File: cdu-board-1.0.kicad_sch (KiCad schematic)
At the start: 18 parts, among them J1 Conn_01x02_Socket, J2 Conn_01x03_Socket, J3 Conn_01x02_Socket, Q1 TIP220G, Q2 TIP220G

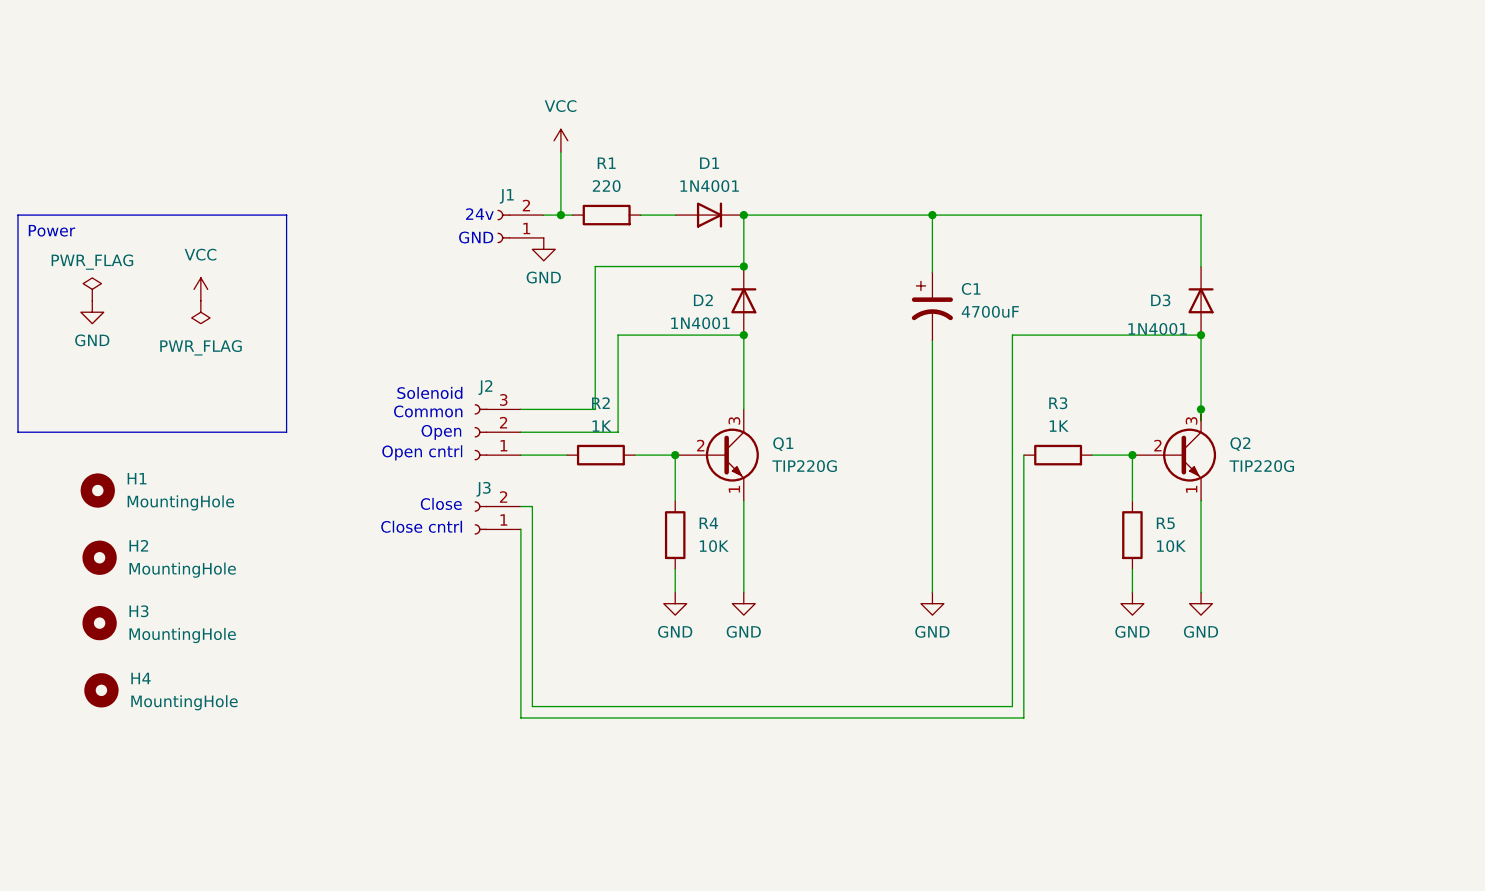
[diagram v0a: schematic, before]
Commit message: Fixed transistor - v1.0 used TIP220G and not TIP120G
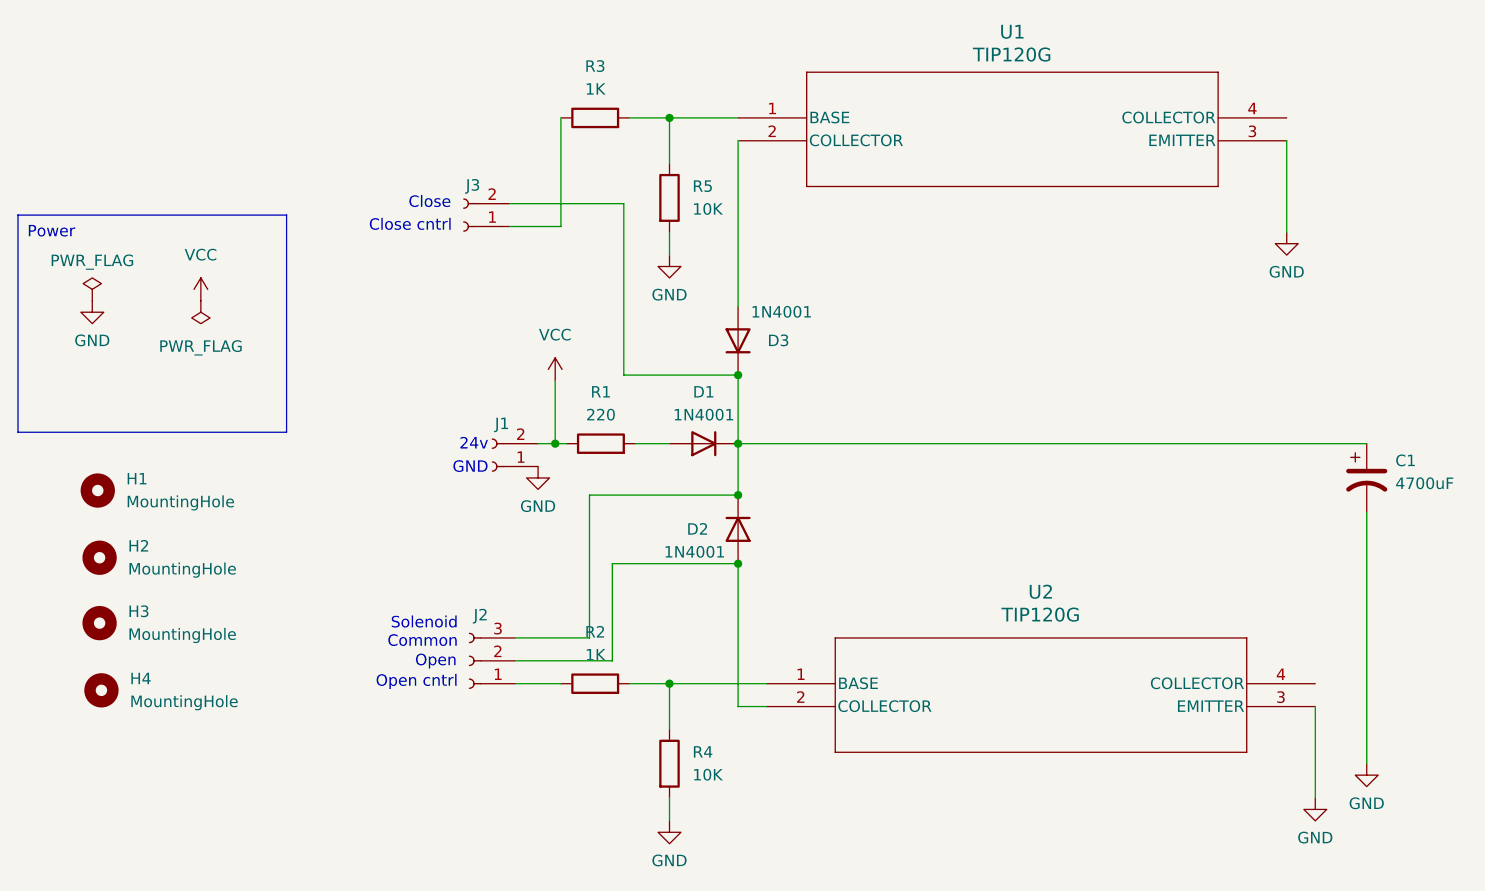
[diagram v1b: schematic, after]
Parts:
- removed Q1, Q2: TIP220G, CDU footprints:TO-220-3_10P53X15P75_ONS, symbol Device:Q_NPN_EBC
- added U1, U2: TIP120G, TO-220-3_10P53X15P75_ONS, symbol cdu-symbols:TIP120G
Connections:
- net GND: now also U1.3 (EMITTER), U2.3 (EMITTER)
- net at C1.1, D1.1 (K), D2.1 (K)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: now also J3.2 (Pin_2)
- net at D3.2 (A): now also U1.2 (COLLECTOR); no longer J3.2 (Pin_2)
- net at R2.2, R4.1: now also U2.1 (BASE)
- net at R3.2, R5.1: now also U1.1 (BASE)
- net at D2.2 (A), J2.2 (Pin_2): now also U2.2 (COLLECTOR)
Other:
- moved on the sheet: C1, D1, D2, D3, J1, J2, J3, R1, R2, R3, R4, R5

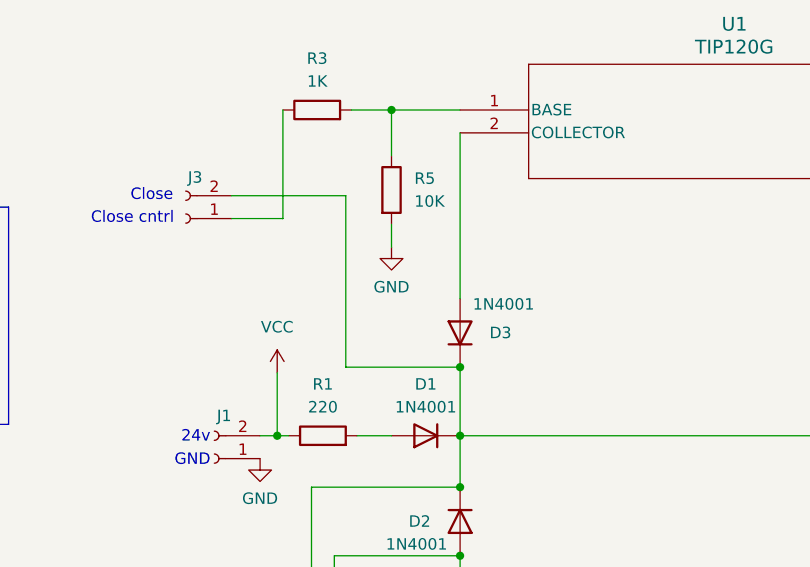
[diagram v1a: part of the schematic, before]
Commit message: Added QR code, fixed an error
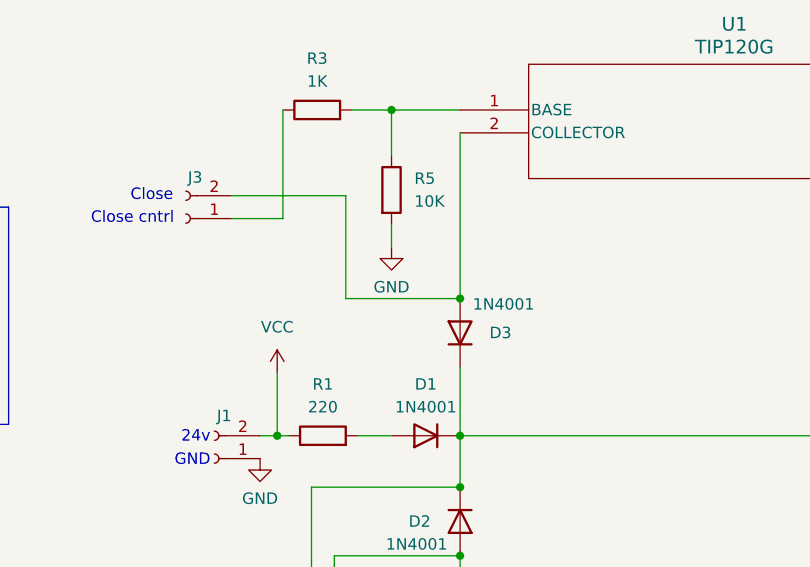
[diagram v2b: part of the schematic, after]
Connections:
- net at C1.1, D1.1 (K), D2.1 (K)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: no longer J3.2 (Pin_2)
- net at D3.2 (A), U1.2 (COLLECTOR): now also J3.2 (Pin_2)
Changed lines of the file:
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@@
   (junction (at 135.255 97.155) (diameter 0) (color 0 0 0 0)
   )
-  (junction (at 135.255 89.535) (diameter 0) (color 0 0 0 0)
+  (junction (at 135.255 102.87) (diameter 0) (color 0 0 0 0)
   )
-  (junction (at 135.255 102.87) (diameter 0) (color 0 0 0 0)
+  (junction (at 135.255 81.915) (diameter 0) (color 0 0 0 0)
   )
   (wire (pts (xy 114.935 90.17) (xy 114.935 97.155))
@@
   )
   (wire (pts (xy 114.935 97.155) (xy 116.205 97.155))
-    (stroke (width 0) (type default))
-  )
-  (wire (pts (xy 122.555 89.535) (xy 135.255 89.535))
     (stroke (width 0) (type default))
   )
@@
     (stroke (width 0) (type default))
   )
-  (wire (pts (xy 122.555 70.485) (xy 122.555 89.535))
-    (stroke (width 0) (type default))
-  )
   (wire (pts (xy 123.825 97.155) (xy 127.635 97.155))
     (stroke (width 0) (type default))
@@
     (stroke (width 0) (type default))
   )
+  (wire (pts (xy 122.555 70.485) (xy 122.555 81.915))
+    (stroke (width 0) (type default))
+  )
+  (wire (pts (xy 135.255 81.915) (xy 122.555 81.915))
+    (stroke (width 0) (type default))
+  )
